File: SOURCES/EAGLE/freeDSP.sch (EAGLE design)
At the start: 118 parts, among them IC1 24AA256P, IC3 AD8608R, Q1 12.288Mhz, Q2 2N7000, Q3 2N7000, Q4 2N7000, Q5 2N7000, T1 FZT751TA, X1 TOBU3, X2 TOBU3, X3 MKDSN1,5/2-5,08, X4 TOBU3, X5 TOBU3, X6 TOBU3, X7 TOBU3

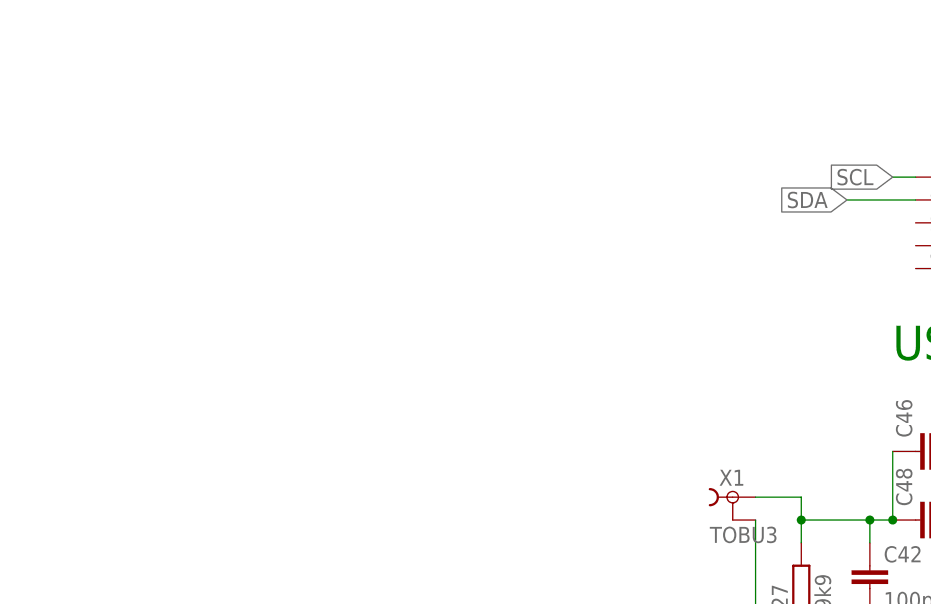
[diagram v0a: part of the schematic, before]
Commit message: Add licensing info to schematic & add PNG-Schematic
This enables users to view the schematic without
the need to download & install EAGLE on their
computer.
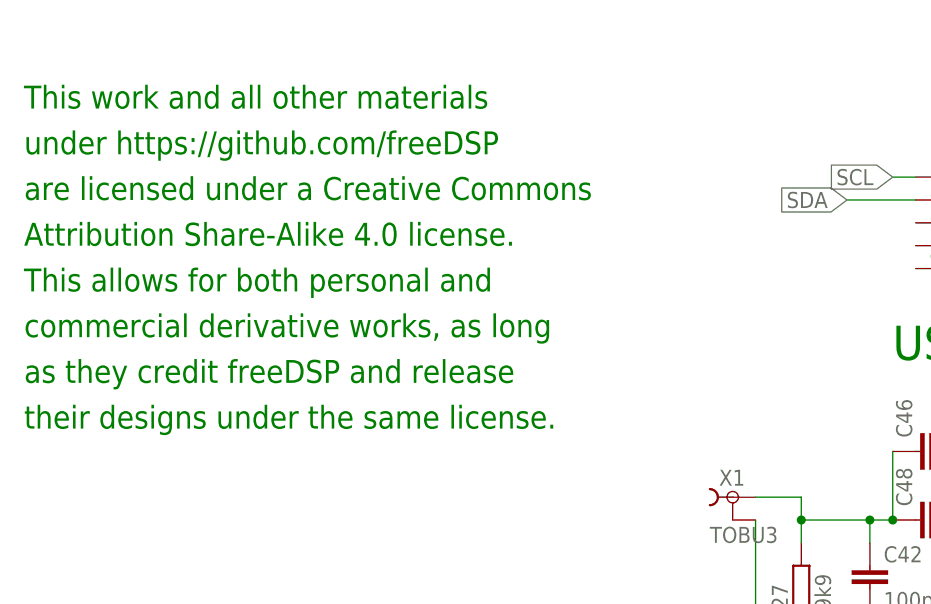
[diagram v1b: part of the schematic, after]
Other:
- note added: "This work and all other materials under https://github.com/freeDSP are licensed under a Creative Commons Attribution Share-Alike 4.0 license. This allows for both personal and commercial derivative works, as long as they credit freeDSP and release their designs under the same license."
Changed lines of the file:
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@@
 <text x="297.18" y="15.24" size="5.08" layer="91">freeDSP 1.1
 www.freedsp.cc</text>
+<text x="-20.32" y="190.5" size="2.54" layer="91" font="vector" distance="100">This work and all other materials
+under https://github.com/freeDSP
+are licensed under a Creative Commons
+Attribution Share-Alike 4.0 license.
+This allows for both personal and
+commercial derivative works, as long
+as they credit freeDSP and release
+their designs under the same license.</text>
 </plain>
 <instances>
